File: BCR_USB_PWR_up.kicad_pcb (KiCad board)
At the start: 2 copper layers, 13.4 x 21.8 mm, 2 parts, among them CN1 DB9_Female, CN2 UE27AC54100

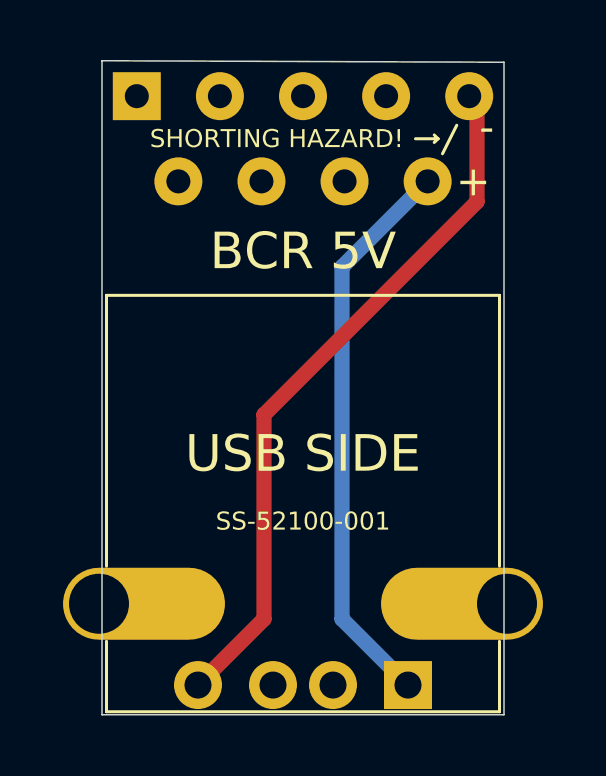
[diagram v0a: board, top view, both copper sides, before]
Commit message: rename NEC to up_long, and a short up version that covers up the shorting hazard
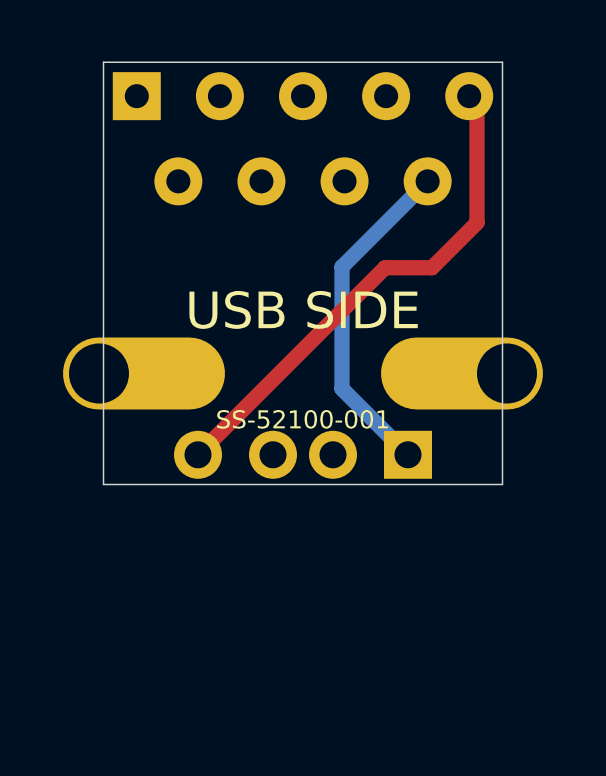
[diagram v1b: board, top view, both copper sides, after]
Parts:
- moved CN2 7.67 mm to (127.0, 103.6)
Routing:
- net /+5V: track 18.9 -> 11.2 mm
- net /GND: track 23.6 -> 16.8 mm
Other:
- board size 13.4 x 21.8 mm -> 13.3 x 14.1 mm
- board text added: "BCR to USB 5v"
- board text removed: "+"
- board text removed: "-"
- board text removed: "5v USB power"
- board text removed: "BCR 5V"
- board text removed: "NEC PC-8201 / PC-8300"
- board text removed: "SHORTING HAZARD!"
- board text removed: "from BCR port"
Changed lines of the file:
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@@
   (general
     (thickness 1.6)
-    (drawings 24)
+    (drawings 14)
     (tracks 8)
     (zones 0)
@@
     (37 F.SilkS user)
     (38 B.Mask user)
-    (39 F.Mask user hide)
+    (39 F.Mask user)
     (40 Dwgs.User user hide)
     (41 Cmts.User user hide)
@@
     (descr "9-pin D-Sub connector, straight/vertical, THT-mount, female, pitch 2.77x2.84mm, distance of mounting holes 25mm, see https://disti-assets.s3.amazonaws.com/tonar/files/datasheets/16730.pdf")
     (tags "9-pin D-Sub connector straight vertical THT female pitch 2.77x2.84mm mounting holes distance 25mm")
-    (fp_text reference CN1 (at -5.5372 1.7018 180) (layer B.SilkS) hide
+    (fp_text reference CN1 (at -5.5372 1.7018) (layer B.SilkS) hide
       (effects (font (size 1 1) (thickness 0.15)) (justify mirror))
     )
-    (fp_text value DB9_Female (at -5.54 -4.53 180) (layer B.Fab)
+    (fp_text value DB9_Female (at -5.54 -4.53) (layer B.Fab)
       (effects (font (size 1 1) (thickness 0.15)) (justify mirror))
     )
-    (fp_text user %R (at -5.54 -1.42 180) (layer B.Fab)
+    (fp_text user %R (at -5.54 -1.42) (layer B.Fab)
       (effects (font (size 1 1) (thickness 0.15)) (justify mirror))
     )
@@
     (fp_line (start -21.04 -6.74) (end 9.96 -6.74) (layer B.CrtYd) (width 0.05))
     (fp_line (start -21.04 3.91) (end -21.04 -6.74) (layer B.CrtYd) (width 0.05))
-    (fp_line (start -10.942952 -5.43) (end -0.137048 -5.43) (layer B.SilkS) (width 0.12))
     (fp_line (start -13.358887 0.652163) (end -12.53015 -4.047837) (layer B.Fab) (width 0.1))
     (fp_line (start 2.278887 0.652163) (end 1.45015 -4.047837) (layer B.Fab) (width 0.1))
     (fp_line (start -10.954457 -5.37) (end -0.125543 -5.37) (layer B.Fab) (width 0.1))
     (fp_line (start -11.783194 2.53) (end 0.703194 2.53) (layer B.Fab) (width 0.1))
-    (fp_arc (start -0.137048 -3.77) (end -0.137048 -5.43) (angle 52.39100523) (layer B.SilkS) (width 0.12))
-    (fp_arc (start -10.942952 -3.77) (end -10.942952 -5.43) (angle -52.80148662) (layer B.SilkS) (width 0.12))
     (fp_arc (start -0.125543 -3.77) (end -0.125543 -5.37) (angle 80) (layer B.Fab) (width 0.1))
     (fp_arc (start -10.954457 -3.77) (end -10.954457 -5.37) (angle -80) (layer B.Fab) (width 0.1))
@@
   )
   (module 0_LOCAL:USB_A_Female_UE27AC54100_cut (layer F.Cu)
-    (at 127 111.258 180)
+    (at 127 103.583 180)
     (fp_text reference CN2 (at 0 -0.889 180 unlocked) (layer F.SilkS) hide
       (effects (font (size 1 1) (thickness 0.15)))
     )
-    (fp_text value UE27AC54100 (at 0 11.35 180) (layer F.Fab)
+    (fp_text value UE27AC54100 (at 0 9.5) (layer F.Fab)
       (effects (font (size 1 1) (thickness 0.15)))
     )
-    (fp_line (start -6.55 -3.6) (end 6.55 -3.6) (layer F.SilkS) (width 0.1))
-    (fp_line (start 6.55 1.25) (end 6.55 10.28) (layer F.SilkS) (width 0.1))
-    (fp_line (start -6.55 1.25) (end -6.55 10.28) (layer F.SilkS) (width 0.1))
-    (fp_line (start -6.55 -3.6) (end -6.55 -1.25) (layer F.SilkS) (width 0.1))
     (fp_line (start -6.55 -3.6) (end 6.55 -3.6) (layer F.Fab) (width 0.1))
     (fp_line (start 6.55 -3.6) (end 6.55 10.28) (layer F.Fab) (width 0.1))
     (fp_line (start -6.55 -3.6) (end -6.55 10.28) (layer F.Fab) (width 0.1))
     (fp_line (start -6.55 10.28) (end 6.55 10.28) (layer F.Fab) (width 0.1))
-    (fp_line (start 6.55 -3.6) (end 6.55 -1.25) (layer F.SilkS) (width 0.1))
-    (fp_line (start 6.55 10.28) (end -6.55 10.28) (layer F.SilkS) (width 0.1))
     (fp_line (start -6.75 -3.94) (end 6.75 -3.94) (layer F.CrtYd) (width 0.05))
     (fp_line (start 6.75 -3.94) (end 6.75 10.375) (layer F.CrtYd) (width 0.05))
     (fp_line (start -6.75 -3.94) (end -6.75 10.375) (layer F.CrtYd) (width 0.05))
     (fp_line (start -6.75 10.375) (end 6.75 10.375) (layer F.CrtYd) (width 0.05))
-    (fp_text user %R (at -0.025 0.975 180) (layer F.Fab)
+    (fp_text user %R (at -0.025 0.975) (layer F.Fab)
       (effects (font (size 1 1) (thickness 0.15)))
     )
@@
     )
   )
-  (gr_line (start 131.5 95.758) (end 131.375 95.633) (layer F.SilkS) (width 0.1016))
-  (gr_line (start 131.5 95.758) (end 131.375 95.883) (layer F.SilkS) (width 0.1016))
-  (gr_line (start 131.5 95.758) (end 130.75 95.758) (layer F.SilkS) (width 0.1016))
-  (gr_line (start 131.65 96.258) (end 132.125 95.308) (layer F.SilkS) (width 0.1016))
-  (gr_text "SHORTING HAZARD!" (at 126.125 95.758) (layer F.SilkS)
-    (effects (font (size 0.6 0.6) (thickness 0.06)))
-  )
-  (gr_text - (at 133.125 95.383) (layer F.SilkS)
-    (effects (font (size 1 1) (thickness 0.1)))
-  )
-  (gr_text + (at 132.675 97.183) (layer F.SilkS)
-    (effects (font (size 1 1) (thickness 0.1)))
-  )
   (gr_text "A-DF 09 PP/Z" (at 127 95.758) (layer B.SilkS)
     (effects (font (size 0.6 0.6) (thickness 0.1)) (justify mirror))
   )
-  (gr_text "from BCR port" (at 126.9 104.658) (layer B.SilkS)
-    (effects (font (size 1 1) (thickness 0.1)) (justify mirror))
-  )
-  (gr_text SS-52100-001 (at 127 108.508) (layer F.SilkS)
+  (gr_text SS-52100-001 (at 127 105.133) (layer F.SilkS)
     (effects (font (size 0.6 0.6) (thickness 0.1)))
   )
-  (gr_text github.com/bkw777/BCR_USB_PWR (at 127.1 109.258) (layer B.SilkS)
+  (gr_text github.com/bkw777/BCR_USB_PWR (at 127 105.158) (layer B.SilkS)
     (effects (font (size 0.5 0.5) (thickness 0.1)) (justify mirror))
   )
-  (gr_text "NEC PC-8201 / PC-8300" (at 127 106.858) (layer B.SilkS)
-    (effects (font (size 0.6 0.6) (thickness 0.1)) (justify mirror))
-  )
-  (gr_text "5v USB power" (at 127 102.958) (layer B.SilkS)
-    (effects (font (size 1 1) (thickness 0.1)) (justify mirror))
-  )
-  (gr_line (start 120.3 93.158) (end 120.3 114.958) (layer Edge.Cuts) (width 0.05))
-  (gr_line (start 133.7 93.208) (end 120.3 93.158) (layer Edge.Cuts) (width 0.05))
-  (gr_line (start 133.7 114.958) (end 133.7 93.208) (layer Edge.Cuts) (width 0.05))
-  (gr_line (start 120.3 114.958) (end 133.7 114.958) (layer Edge.Cuts) (width 0.05))
+  (gr_text "BCR to USB 5v" (at 127 101.508) (layer B.SilkS)
+    (effects (font (size 1.2 1) (thickness 0.2)) (justify mirror))
+  )
+  (gr_line (start 120.35 93.208) (end 120.35 107.283) (layer Edge.Cuts) (width 0.05))
+  (gr_line (start 133.65 93.208) (end 120.35 93.208) (layer Edge.Cuts) (width 0.05))
+  (gr_line (start 133.65 107.283) (end 133.65 93.208) (layer Edge.Cuts) (width 0.05))
+  (gr_line (start 120.35 107.283) (end 133.65 107.283) (layer Edge.Cuts) (width 0.05))
   (gr_line (start 125 114.258) (end 129 114.258) (layer Dwgs.User) (width 0.0254))
   (gr_line (start 127 97.258) (end 127 114.258) (layer Dwgs.User) (width 0.0254))
   (gr_line (start 114.3 87.376) (end 139.7 104.14) (layer Dwgs.User) (width 0.0254))
   (gr_line (start 114.3 104.14) (end 139.7 87.376) (layer Dwgs.User) (width 0.0254))
-  (gr_text "BCR 5V" (at 127 99.508) (layer F.SilkS)
-    (effects (font (size 1.2192 1.2192) (thickness 0.2032)))
-  )
   (gr_text "DE9F SIDE" (at 127 98.908) (layer B.SilkS)
     (effects (font (size 1 1) (thickness 0.16)) (justify mirror))
   )
-  (gr_text "USB SIDE" (at 127 106.258) (layer F.SilkS)
+  (gr_text "USB SIDE" (at 127 101.508) (layer F.SilkS)
     (effects (font (size 1.2192 1.2192) (thickness 0.2032)))
   )
-  (segment (start 128.3 111.768) (end 130.5 113.968) (width 0.508) (layer B.Cu) (net 1))
+  (segment (start 128.3 104.093) (end 130.5 106.293) (width 0.508) (layer B.Cu) (net 1))
   (segment (start 131.15526 97.17814) (end 128.3 100.0334) (width 0.508) (layer B.Cu) (net 1))
-  (segment (start 128.3 100.0334) (end 128.3 111.768) (width 0.508) (layer B.Cu) (net 1))
-  (segment (start 132.8 97.858) (end 132.8 94.59788) (width 0.508) (layer F.Cu) (net 2))
-  (segment (start 125.7 104.958) (end 132.8 97.858) (width 0.508) (layer F.Cu) (net 2))
-  (segment (start 123.5 113.968) (end 125.7 111.768) (width 0.508) (layer F.Cu) (net 2))
+  (segment (start 128.3 100.0334) (end 128.3 104.093) (width 0.508) (layer B.Cu) (net 1))
   (segment (start 132.8 94.59788) (end 132.54026 94.33814) (width 0.508) (layer F.Cu) (net 2))
-  (segment (start 125.7 111.768) (end 125.7 104.958) (width 0.508) (layer F.Cu) (net 2))
+  (segment (start 132.8 98.558) (end 132.8 94.59788) (width 0.508) (layer F.Cu) (net 2))
+  (segment (start 131.3 100.058) (end 132.8 98.558) (width 0.508) (layer F.Cu) (net 2))
+  (segment (start 123.5 106.293) (end 129.735 100.058) (width 0.508) (layer F.Cu) (net 2))
+  (segment (start 129.735 100.058) (end 131.3 100.058) (width 0.508) (layer F.Cu) (net 2))
 )

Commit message: Add BCR_Breakout. Rename repo to BCR_Breakout.
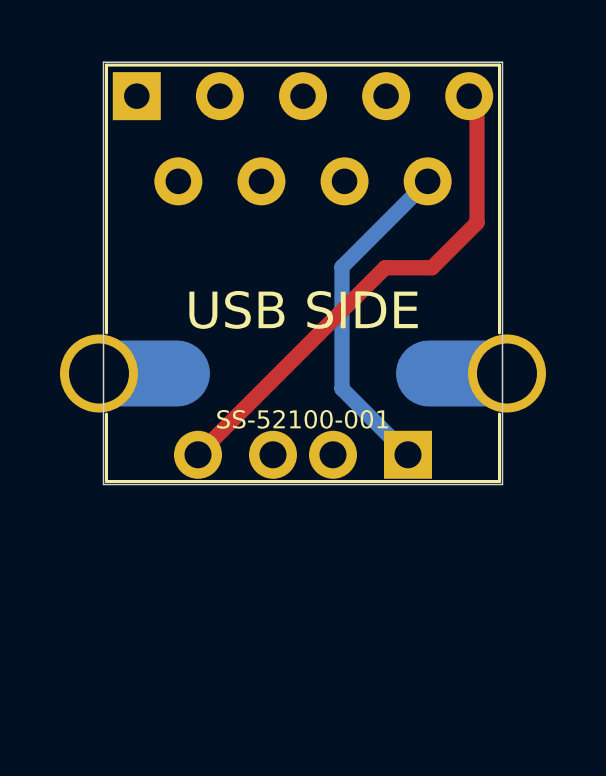
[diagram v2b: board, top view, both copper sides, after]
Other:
- board text added: "github.com/bkw777/BCR_Breakout"
- board text removed: "github.com/bkw777/BCR_USB_PWR"
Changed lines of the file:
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@@
     (descr "9-pin D-Sub connector, straight/vertical, THT-mount, female, pitch 2.77x2.84mm, distance of mounting holes 25mm, see https://disti-assets.s3.amazonaws.com/tonar/files/datasheets/16730.pdf")
     (tags "9-pin D-Sub connector straight vertical THT female pitch 2.77x2.84mm mounting holes distance 25mm")
-    (fp_text reference CN1 (at -5.5372 1.7018) (layer B.SilkS) hide
+    (fp_text reference CN1 (at -5.5372 1.7018 180) (layer B.SilkS) hide
       (effects (font (size 1 1) (thickness 0.15)) (justify mirror))
     )
-    (fp_text value DB9_Female (at -5.54 -4.53) (layer B.Fab)
+    (fp_text value DB9_Female (at -5.54 -4.53 180) (layer B.Fab)
       (effects (font (size 1 1) (thickness 0.15)) (justify mirror))
     )
-    (fp_text user %R (at -5.54 -1.42) (layer B.Fab)
+    (fp_text user %R (at -5.54 -1.42 180) (layer B.Fab)
       (effects (font (size 1 1) (thickness 0.15)) (justify mirror))
     )
@@
     (fp_line (start -5.54 -0.82) (end -5.54 -2.02) (layer Dwgs.User) (width 0.01))
     (fp_line (start -6.54 -1.42) (end -4.54 -1.42) (layer Dwgs.User) (width 0.01))
-    (pad 9 thru_hole circle (at -9.695 -2.84 180) (size 1.6 1.6) (drill 0.8) (layers *.Cu *.Mask)
+    (pad 9 thru_hole circle (at -9.695 -2.84 180) (size 1.6 1.6) (drill 0.85) (layers *.Cu *.Mask)
       (net 1 /+5V))
-    (pad 8 thru_hole circle (at -6.925 -2.84 180) (size 1.6 1.6) (drill 0.8) (layers *.Cu *.Mask))
-    (pad 7 thru_hole circle (at -4.155 -2.84 180) (size 1.6 1.6) (drill 0.8) (layers *.Cu *.Mask))
-    (pad 6 thru_hole circle (at -1.385 -2.84 180) (size 1.6 1.6) (drill 0.8) (layers *.Cu *.Mask))
-    (pad 5 thru_hole circle (at -11.08 0 180) (size 1.6 1.6) (drill 0.8) (layers *.Cu *.Mask)
+    (pad 8 thru_hole circle (at -6.925 -2.84 180) (size 1.6 1.6) (drill 0.85) (layers *.Cu *.Mask))
+    (pad 7 thru_hole circle (at -4.155 -2.84 180) (size 1.6 1.6) (drill 0.85) (layers *.Cu *.Mask))
+    (pad 6 thru_hole circle (at -1.385 -2.84 180) (size 1.6 1.6) (drill 0.85) (layers *.Cu *.Mask))
+    (pad 5 thru_hole circle (at -11.08 0 180) (size 1.6 1.6) (drill 0.85) (layers *.Cu *.Mask)
       (net 2 /GND))
-    (pad 4 thru_hole circle (at -8.31 0 180) (size 1.6 1.6) (drill 0.8) (layers *.Cu *.Mask))
-    (pad 3 thru_hole circle (at -5.54 0 180) (size 1.6 1.6) (drill 0.8) (layers *.Cu *.Mask))
-    (pad 2 thru_hole circle (at -2.77 0 180) (size 1.6 1.6) (drill 0.8) (layers *.Cu *.Mask))
-    (pad 1 thru_hole rect (at 0 0 180) (size 1.6 1.6) (drill 0.8) (layers *.Cu *.Mask))
+    (pad 4 thru_hole circle (at -8.31 0 180) (size 1.6 1.6) (drill 0.85) (layers *.Cu *.Mask))
+    (pad 3 thru_hole circle (at -5.54 0 180) (size 1.6 1.6) (drill 0.85) (layers *.Cu *.Mask))
+    (pad 2 thru_hole circle (at -2.77 0 180) (size 1.6 1.6) (drill 0.85) (layers *.Cu *.Mask))
+    (pad 1 thru_hole rect (at 0 0 180) (size 1.6 1.6) (drill 0.85) (layers *.Cu *.Mask))
     (model ${KIPRJMOD}/3dmodels/DE9F_metal.step
       (offset (xyz -5.54 -1.42 6.3))
@@
       (effects (font (size 1 1) (thickness 0.15)))
     )
+    (fp_line (start -6.55 -3.6) (end 6.55 -3.6) (layer F.SilkS) (width 0.1))
+    (fp_line (start 6.55 1.35) (end 6.55 10.28) (layer F.SilkS) (width 0.1))
+    (fp_line (start -6.55 1.35) (end -6.55 10.28) (layer F.SilkS) (width 0.1))
+    (fp_line (start -6.55 -3.6) (end -6.55 -1.35) (layer F.SilkS) (width 0.1))
     (fp_line (start -6.55 -3.6) (end 6.55 -3.6) (layer F.Fab) (width 0.1))
     (fp_line (start 6.55 -3.6) (end 6.55 10.28) (layer F.Fab) (width 0.1))
     (fp_line (start -6.55 -3.6) (end -6.55 10.28) (layer F.Fab) (width 0.1))
     (fp_line (start -6.55 10.28) (end 6.55 10.28) (layer F.Fab) (width 0.1))
+    (fp_line (start 6.55 -3.6) (end 6.55 -1.35) (layer F.SilkS) (width 0.1))
+    (fp_line (start 6.55 10.28) (end -6.55 10.28) (layer F.SilkS) (width 0.1))
     (fp_line (start -6.75 -3.94) (end 6.75 -3.94) (layer F.CrtYd) (width 0.05))
     (fp_line (start 6.75 -3.94) (end 6.75 10.375) (layer F.CrtYd) (width 0.05))
@@
       (effects (font (size 1 1) (thickness 0.15)))
     )
+    (pad SH smd oval (at 7 0 180) (size 4.8 2.2) (drill (offset -1.5 0)) (layers B.Cu B.Paste B.Mask)
+      (net 3 "Net-(CN2-PadSH)"))
+    (pad SH smd oval (at -7 0 180) (size 4.8 2.2) (drill (offset 1.5 0)) (layers B.Cu B.Paste B.Mask)
+      (net 3 "Net-(CN2-PadSH)"))
     (pad 4 thru_hole circle (at 3.5 -2.71 180) (size 1.6 1.6) (drill 0.9) (layers *.Cu *.Mask)
       (net 2 /GND))
@@
     (pad 1 thru_hole rect (at -3.5 -2.71 180) (size 1.6 1.6) (drill 0.9) (layers *.Cu *.Mask)
       (net 1 /+5V))
-    (pad SH thru_hole oval (at 6.8 0 180) (size 5.4 2.4) (drill 2 (offset -1.5 0)) (layers *.Cu *.Mask)
+    (pad SH thru_hole circle (at 6.8 0 180) (size 2.6 2.6) (drill 2) (layers *.Cu *.Mask)
       (net 3 "Net-(CN2-PadSH)"))
-    (pad SH thru_hole oval (at -6.8 0 180) (size 5.4 2.4) (drill 2 (offset 1.5 0)) (layers *.Cu *.Mask)
+    (pad SH thru_hole circle (at -6.8 0 180) (size 2.6 2.6) (drill 2) (layers *.Cu *.Mask)
       (net 3 "Net-(CN2-PadSH)"))
     (model ${KIPRJMOD}/3dmodels/USB-A_female_horiz_thru.step
@@
     (effects (font (size 0.6 0.6) (thickness 0.1)))
   )
-  (gr_text github.com/bkw777/BCR_USB_PWR (at 127 105.158) (layer B.SilkS)
+  (gr_text github.com/bkw777/BCR_Breakout (at 127 105.158) (layer B.SilkS)
     (effects (font (size 0.5 0.5) (thickness 0.1)) (justify mirror))
   )
